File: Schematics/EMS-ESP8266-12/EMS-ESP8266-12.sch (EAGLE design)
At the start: 44 parts, among them IC1 LM393N, T1 BC547B, T2 BC547B

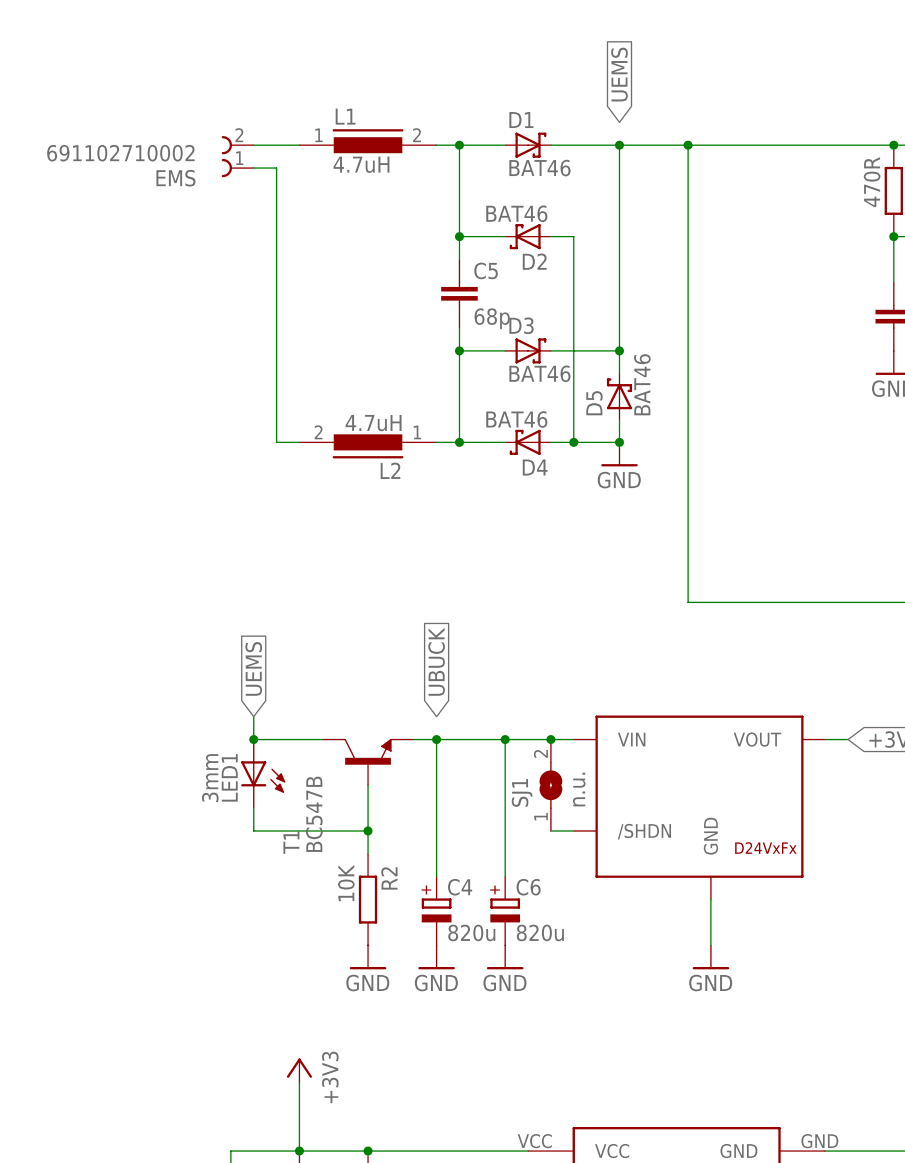
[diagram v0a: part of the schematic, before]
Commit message: EMS-ESP86266/12 Rev 1.0c
- Basiswiderstand R14 (10k) zur Strombegrenzung
- Package für T1,T2 in TO92 geändert
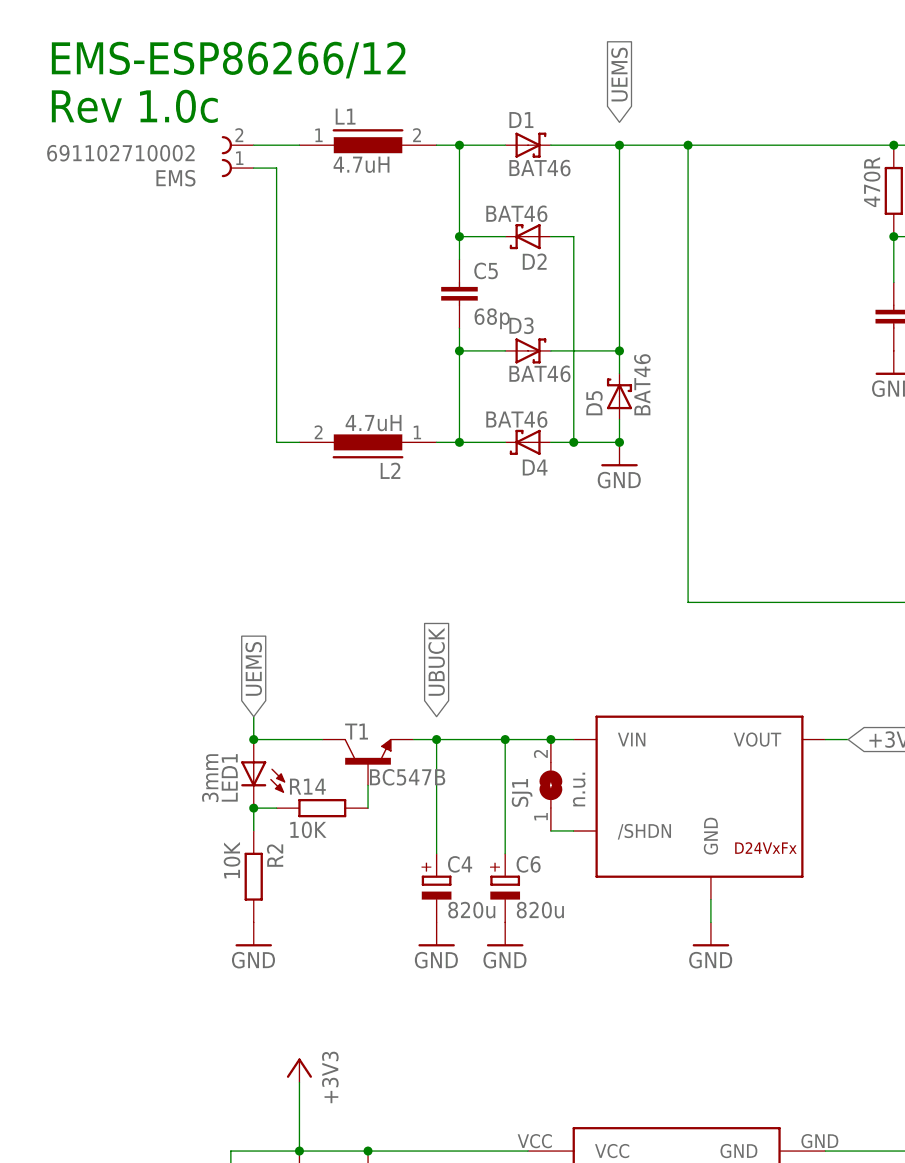
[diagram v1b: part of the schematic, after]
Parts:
- added R14: 10K, resistor:R-EU_0204/7
- T1, T2: device transistor:-NPN-TO92-EBC -> transistor:-NPN-TO92
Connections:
- new net N$10: R14.2, T1.B
- net N$17: now also R14.1; no longer T1.B
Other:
- note added: "EMS-ESP86266/12 Rev 1.0c"
- moved on the sheet: C4, C6, R2
